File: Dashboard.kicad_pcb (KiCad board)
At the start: 2 copper layers, 176.5 x 121.5 mm, 160 parts, among them J1 Left_Signal, J10 AccelConn, J11 BrakeConn, J12 AccelConn2, J13 BrakeConn2, J14 Motor-P, J15 Motor-C, J16 Array-C, J17 Array-P, J18 PowerConn, J19 CAN_OUT, J2 Right_Signal, J20 MotorCANConnector, J21 CAN_IN, J22 CAN_OUT, J23 USB_B_Micro, J24 ExtraGPIO_Conn, J25 UART_TP, J26 CAN_TP, J27 CAN_TP, J3 Brake Light, J4 Headlight, J5 MinionConn, J6 SPI, J7 BPS_PWR, J8 JTAG, SW10 RESET, SW8 SW_Rotary2x6, SW9 KILL_SW, U1 EL3H7, U10 EL3H7, U11 EL3H7, U12 RI3-1205S, U13 NCP1117-3.3_SOT223, U14 ADM3055E, U15 CDSOT23-T24CAN, U16 LTC6820, U17 ADM3055E, U18 CDSOT23-T24CAN, U19 CP2102N-A01-GQFN24, U2 EL3H7, U20 HX1188FNL, U3 EL3H7, U4 EL3H7, U5 EL3H7, U6 EL3H7, U7 STM32F413RHTx, U8 EL3H7, U9 EL3H7, Y1 Crystal

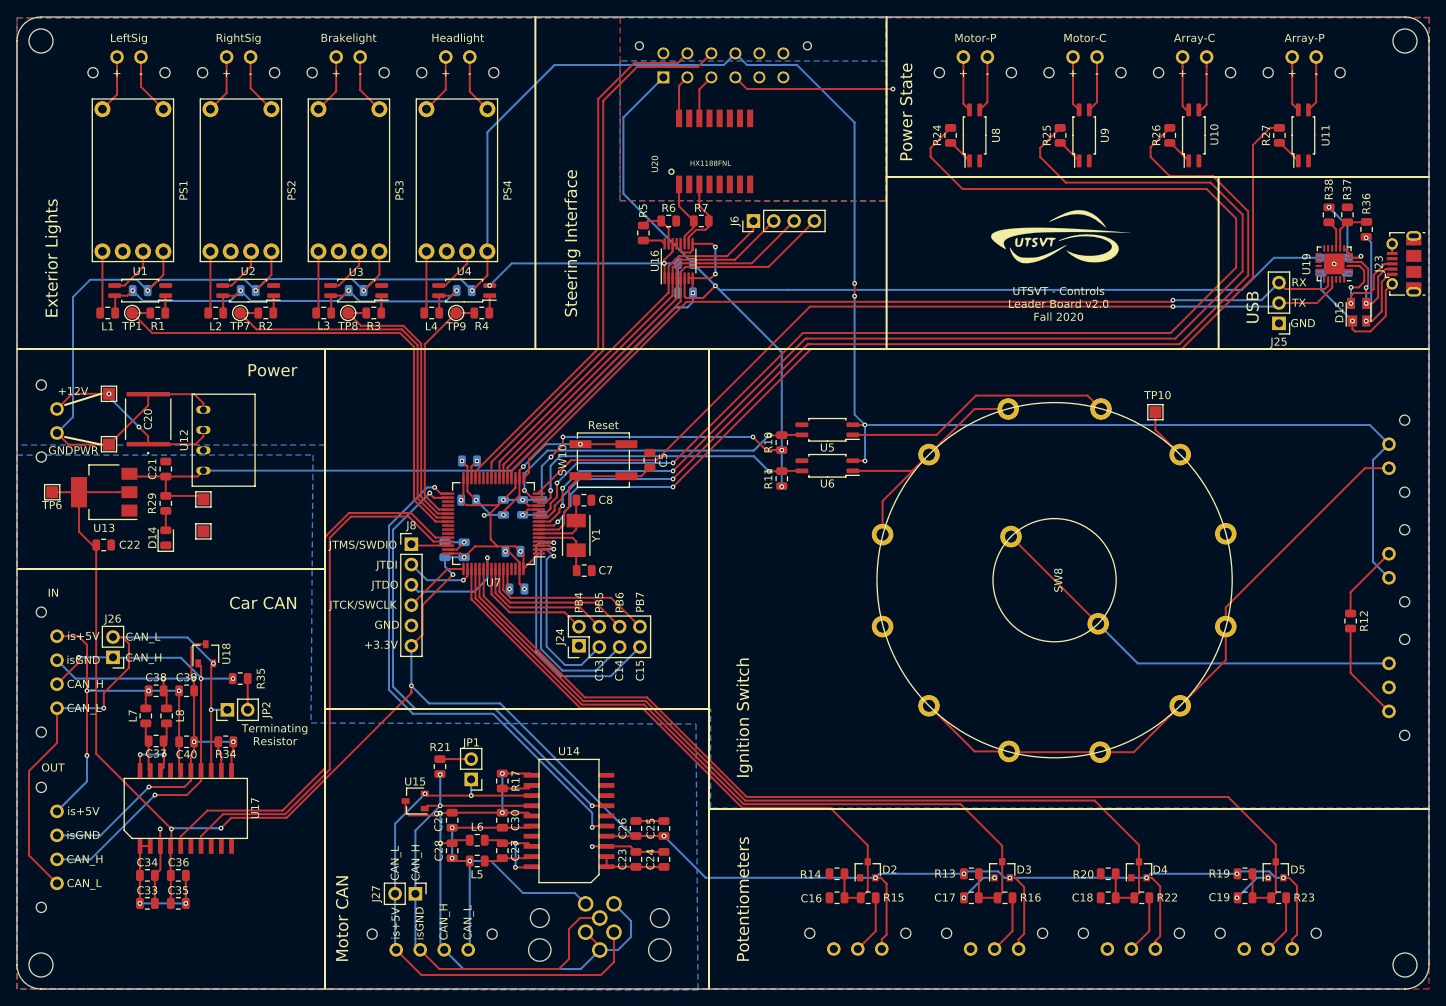
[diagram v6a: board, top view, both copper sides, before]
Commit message: Finishes label and redesigns emergency switch/error light circuitry
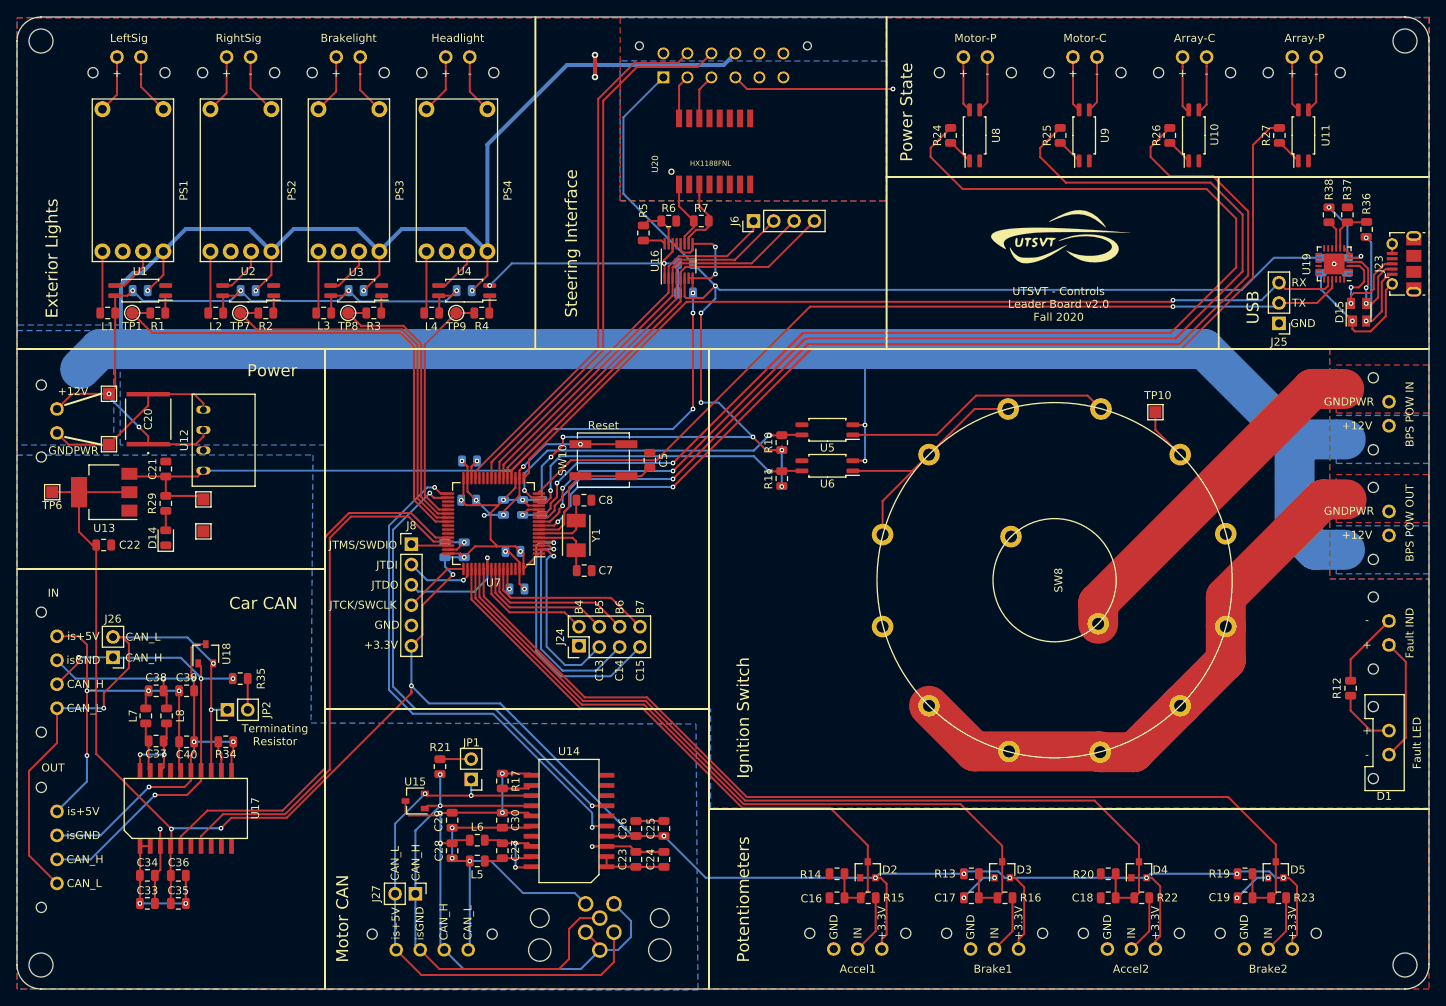
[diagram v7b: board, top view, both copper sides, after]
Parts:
- removed SW9: KILL_SW, UTSVT_Connectors:Molex_MicroFit3.0_1x3xP3.00mm_PolarizingPeg_Vertical
- added J28: KILL_SW_IND, UTSVT_Connectors:Molex_MicroFit3.0_1x2xP3.00mm_PolarizingPeg_Vertical, B.Cu at (202.5, 129.0)
- added J9: BPS_PWR_IN, UTSVT_Connectors:Molex_MicroFit3.0_1x2xP3.00mm_PolarizingPeg_Vertical, B.Cu at (202.5, 101.6)
- D1: moved to F.Cu
- J7: value BPS_PWR -> BPS_PWR_OUT
- moved D1 22.1 mm to (202.5, 145.7)
- moved R12 8.40 mm to (197.7, 137.4), turned to 270 degrees
- moved J7 5.40 mm to (202.5, 115.3), turned to 270 degrees
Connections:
- D1 pad 1: GNDPWR -> Net-(D1-Pad1)
- SW8 pad 13: Net-(SW8-Pad13) -> Net-(J9-Pad1)
- SW8 pad 14: Net-(SW8-Pad13) -> +12V
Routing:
- net Net-(SW8-Pad13): track 53.8 -> 0.00 mm
- net Net-(J9-Pad1): track 0.00 -> 44.4 mm
- net GNDPWR: track 318.4 -> 357.6 mm, vias 8 -> 6
- net Net-(D1-Pad1): track 0.00 -> 15.4 mm
- net /BPS_PWR: track 78.5 -> 92.2 mm
- net +12V: track 86.2 -> 99.4 mm, vias 6 -> 8
- net +5V: track 122.0 -> 132.1 mm, vias 5 -> 7
- net Net-(J28-Pad1): track 12.4 -> 9.45 mm
- net Net-(D1-Pad2): track 9.45 -> 7.70 mm
- net +3V3: track 532.8 -> 533.1 mm, vias 24 -> 26
- added copper zone on F.Cu, net /BPS_PWR
- added copper zone on B.Cu, net GNDPWR
- added copper zone on F.Cu, net Net-(J9-Pad1)
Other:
- board text added: "Accel1"
- board text added: "Accel2"
- board text added: "B4"
- board text added: "B5"
- board text added: "B6"
- board text added: "B7"
- board text added: "BPS POW IN"
- board text added: "BPS POW OUT"
- board text added: "Brake1"
- board text added: "Brake2"
- board text added: "Fault IND"
- board text added: "Fault LED"
- board text added: "Warning: pay careful attention to +/- labels"
- board text removed: "PB4"
- board text removed: "PB5"
- board text removed: "PB6"
- board text removed: "PB7"

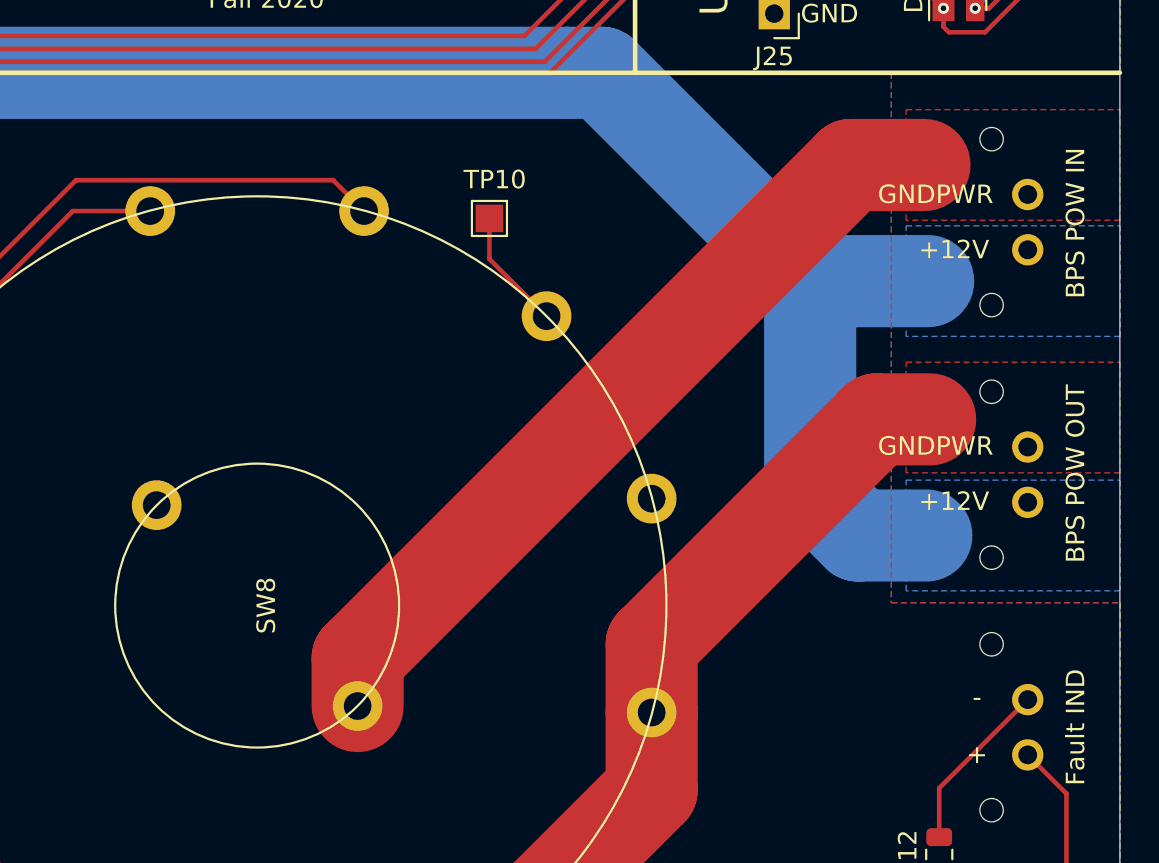
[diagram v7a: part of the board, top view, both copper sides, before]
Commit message: Adds connector for power secondary board
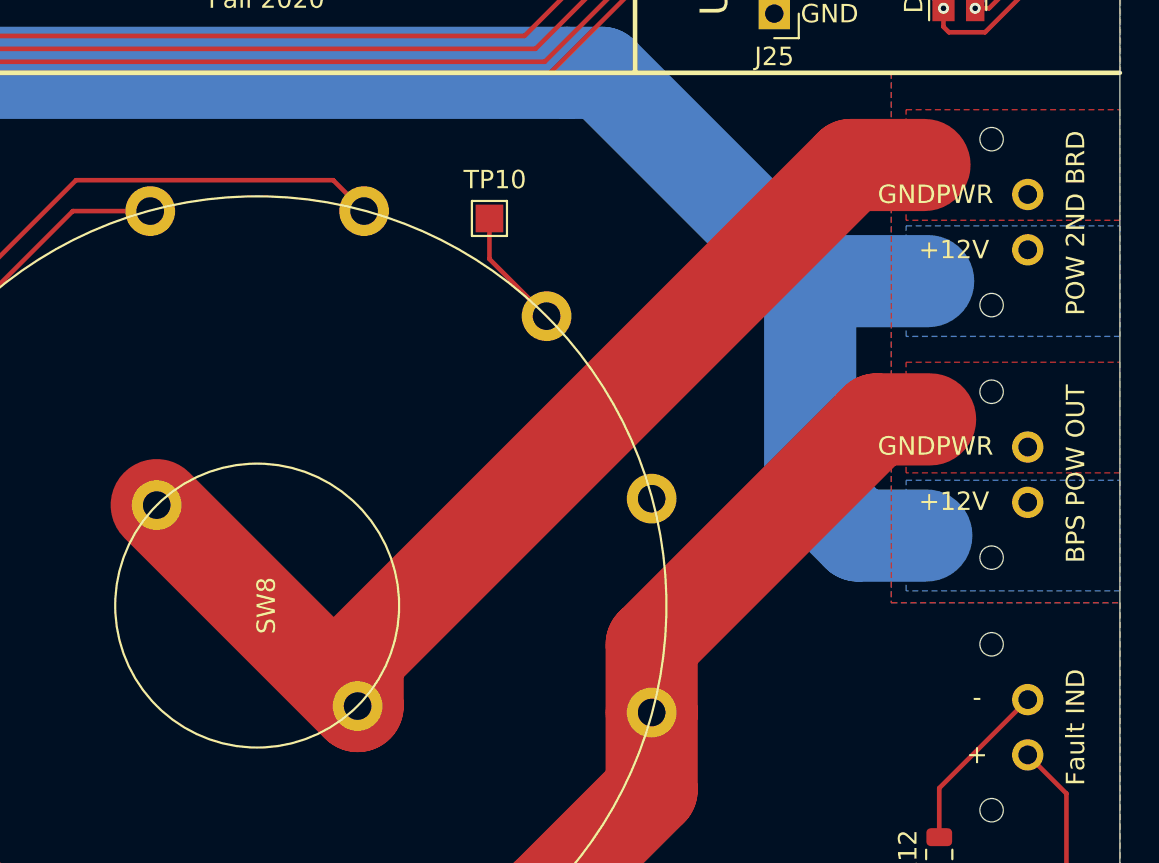
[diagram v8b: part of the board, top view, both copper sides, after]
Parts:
- J9: value BPS_PWR_IN -> POW_2ND_CONN
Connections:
- SW8 pad 14: +12V -> Net-(J9-Pad1)
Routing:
- net Net-(J9-Pad1): track 44.4 -> 59.8 mm
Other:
- board text added: "POW 2ND BRD"
- board text removed: "BPS POW IN"
